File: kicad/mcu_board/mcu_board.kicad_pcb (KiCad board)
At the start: 2 copper layers, 20.3 x 71.1 mm, 25 parts, among them J1 Conn_02x08_Odd_Even, J2 Conn_02x05_Odd_Even, U1 STM32G431CBTx, U2 LD2985BM33R, Y1 ECS-327TXO-33-TR

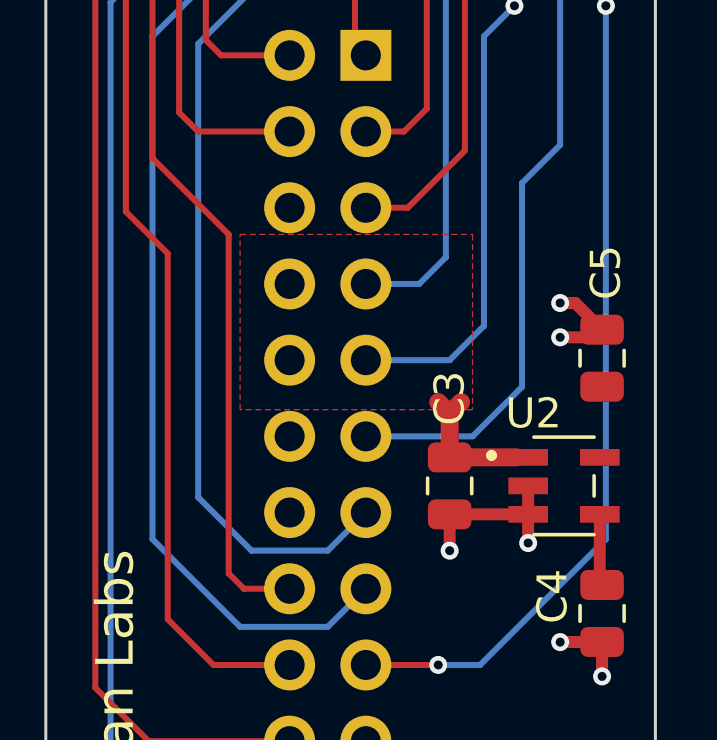
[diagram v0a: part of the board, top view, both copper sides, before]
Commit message: fix LDO bug. FW updates to support new HW
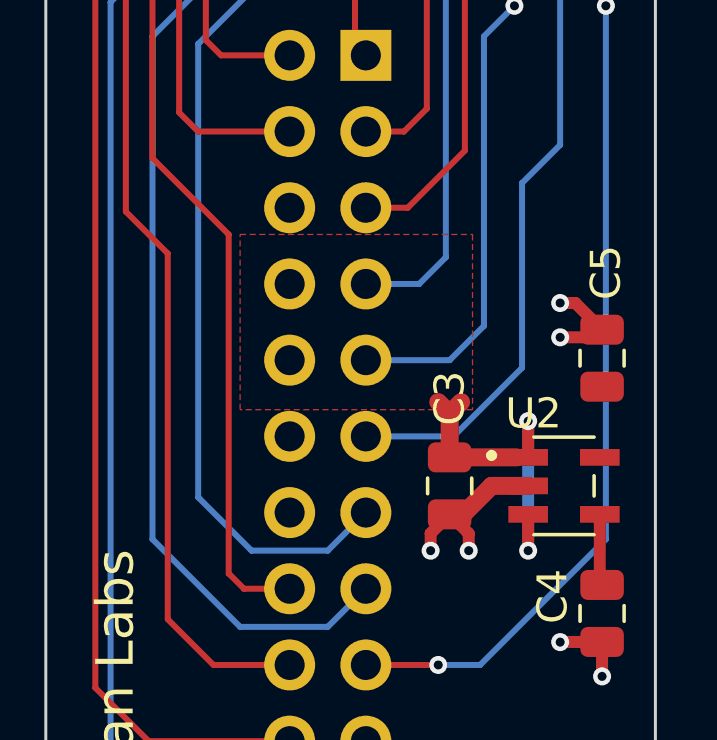
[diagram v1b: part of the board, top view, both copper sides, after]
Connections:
- U2 pad 3: GND -> +5V
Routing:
- net +5V: track 4.78 -> 11.4 mm, vias 0 -> 2
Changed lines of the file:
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@@
       (net 1 "GND") (pinfunction "GND") (pintype "power_in"))
     (pad "3" smd rect (at 1.1938 -0.950001) (size 1.3208 0.5588) (layers "F.Cu" "F.Paste" "F.Mask")
-      (net 1 "GND") (pinfunction "INHIBIT") (pintype "bidirectional"))
+      (net 2 "+5V") (pinfunction "INHIBIT") (pintype "bidirectional"))
     (pad "4" smd rect (at -1.1938 -0.950001) (size 1.3208 0.5588) (layers "F.Cu" "F.Paste" "F.Mask")
       (net 44 "Net-(U2-BYPASS)") (pinfunction "BYPASS") (pintype "unspecified"))
@@
   )
   (segment (start 149.159 68.374) (end 149.111 68.326) (width 0.4) (layer "F.Cu") (net 1))
-  (segment (start 147.193 91.247) (end 147.193 92.456) (width 0.4) (layer "F.Cu") (net 1))
+  (segment (start 148.59 90.297) (end 149.8092 90.297) (width 0.6) (layer "F.Cu") (net 1))
   (segment (start 140.335 55.359) (end 140.335 53.975) (width 0.4) (layer "F.Cu") (net 1))
+  (segment (start 146.558 91.882) (end 147.193 91.247) (width 0.4) (layer "F.Cu") (net 1))
+  (segment (start 146.558 92.456) (end 146.558 91.882) (width 0.4) (layer "F.Cu") (net 1))
   (segment (start 150.876 95.504) (end 150.881 95.499) (width 0.4) (layer "F.Cu") (net 1))
   (segment (start 147.538 64.516) (end 147.538 66.1385) (width 0.3) (layer "F.Cu") (net 1))
@@
   (segment (start 140.335 55.359) (end 141.478 55.359) (width 0.4) (layer "F.Cu") (net 1))
   (segment (start 137.922 53.467) (end 139.253 53.467) (width 0.4) (layer "F.Cu") (net 1))
-  (segment (start 147.193 91.247) (end 149.8092 91.247001) (width 0.4) (layer "F.Cu") (net 1))
+  (segment (start 147.64 91.247) (end 148.59 90.297) (width 0.6) (layer "F.Cu") (net 1))
   (segment (start 136.525 53.467) (end 137.856 53.467) (width 0.4) (layer "F.Cu") (net 1))
   (segment (start 149.032 70.612) (end 149.032 72.009) (width 0.4) (layer "F.Cu") (net 1))
   (segment (start 149.159 70.612) (end 149.159 68.374) (width 0.4) (layer "F.Cu") (net 1))
-  (segment (start 149.8092 91.247001) (end 149.8092 92.202) (width 0.4) (layer "F.Cu") (net 1))
   (segment (start 151.384 84.201) (end 152.273 85.09) (width 0.4) (layer "F.Cu") (net 1))
+  (segment (start 147.193 91.247) (end 147.64 91.247) (width 0.6) (layer "F.Cu") (net 1))
   (segment (start 136.108 61.468) (end 136.108 60.228) (width 0.4) (layer "F.Cu") (net 1))
   (segment (start 150.881 95.499) (end 152.273 95.499) (width 0.4) (layer "F.Cu") (net 1))
@@
   (segment (start 145.034 64.516) (end 145.538 65.024) (width 0.3) (layer "F.Cu") (net 1))
   (segment (start 149.0725 103.124) (end 147.574 103.124) (width 0.2) (layer "F.Cu") (net 1))
+  (segment (start 147.828 92.456) (end 147.828 91.882) (width 0.4) (layer "F.Cu") (net 1))
   (segment (start 150.876 84.201) (end 151.384 84.201) (width 0.4) (layer "F.Cu") (net 1))
-  (segment (start 149.8092 91.247001) (end 149.8092 90.297) (width 0.4) (layer "F.Cu") (net 1))
   (segment (start 149.111 67.678) (end 149.111 68.326) (width 0.4) (layer "F.Cu") (net 1))
   (segment (start 149.606 67.183) (end 149.111 67.678) (width 0.4) (layer "F.Cu") (net 1))
@@
   (segment (start 140.335 53.975) (end 139.827 53.467) (width 0.4) (layer "F.Cu") (net 1))
   (segment (start 150.876 85.344) (end 152.019 85.344) (width 0.4) (layer "F.Cu") (net 1))
+  (segment (start 147.828 91.882) (end 147.193 91.247) (width 0.4) (layer "F.Cu") (net 1))
   (segment (start 152.273 95.499) (end 152.273 96.647) (width 0.4) (layer "F.Cu") (net 1))
   (segment (start 148.173 59.726) (end 149.4505 59.726) (width 0.3) (layer "F.Cu") (net 1))
@@
   (via (at 136.108 61.468) (size 0.6) (drill 0.3) (layers "F.Cu" "B.Cu") (net 1))
   (via (at 151.27 56.007) (size 0.6) (drill 0.3) (layers "F.Cu" "B.Cu") (free) (net 1))
-  (via (at 149.8092 92.202) (size 0.6) (drill 0.3) (layers "F.Cu" "B.Cu") (net 1))
   (via (at 143.51 59.436) (size 0.6) (drill 0.3) (layers "F.Cu" "B.Cu") (free) (net 1))
   (via (at 147.538 64.516) (size 0.6) (drill 0.3) (layers "F.Cu" "B.Cu") (free) (net 1))
@@
   (via (at 147.955 45.085) (size 0.6) (drill 0.3) (layers "F.Cu" "B.Cu") (net 1))
   (via (at 139.319 53.467) (size 0.6) (drill 0.3) (layers "F.Cu" "B.Cu") (free) (net 1))
-  (via (at 147.193 92.456) (size 0.6) (drill 0.3) (layers "F.Cu" "B.Cu") (net 1))
+  (via (at 146.558 92.456) (size 0.6) (drill 0.3) (layers "F.Cu" "B.Cu") (free) (net 1))
+  (via (at 147.828 92.456) (size 0.6) (drill 0.3) (layers "F.Cu" "B.Cu") (free) (net 1))
   (segment (start 147.193 89.347) (end 149.4282 89.346999) (width 0.6) (layer "F.Cu") (net 2))
+  (segment (start 149.8092 89.346999) (end 149.8092 88.138) (width 0.4) (layer "F.Cu") (net 2))
+  (segment (start 149.8092 91.247001) (end 149.8092 92.456) (width 0.4) (layer "F.Cu") (net 2))
   (segment (start 147.193 89.347) (end 147.193 87.884) (width 0.6) (layer "F.Cu") (net 2))
   (segment (start 147.193 87.884) (end 147.574 87.503) (width 0.6) (layer "F.Cu") (net 2))
   (segment (start 147.193 87.884) (end 146.812 87.503) (width 0.6) (layer "F.Cu") (net 2))
+  (via (at 149.8092 92.456) (size 0.6) (drill 0.3) (layers "F.Cu" "B.Cu") (free) (net 2))
+  (via (at 149.8092 88.138) (size 0.6) (drill 0.3) (layers "F.Cu" "B.Cu") (free) (net 2))
+  (segment (start 149.8092 88.138) (end 149.8092 92.329) (width 0.4) (layer "B.Cu") (net 2))
   (segment (start 139.065 75.438) (end 139.065 65.532) (width 0.2) (layer "F.Cu") (net 3))
   (segment (start 139.871 64.726) (end 141.1255 64.726) (width 0.2) (layer "F.Cu") (net 3))
@@
   (segment (start 151.094 64.226) (end 149.4505 64.226) (width 0.2) (layer "F.Cu") (net 11))
   (via (at 150.876 73.406) (size 0.6) (drill 0.3) (layers "F.Cu" "B.Cu") (net 11))
-  (segment (start 149.606 86.995) (end 147.955 88.646) (width 0.2) (layer "B.Cu") (net 11))
+  (segment (start 149.606 86.36) (end 147.32 88.646) (width 0.2) (layer "B.Cu") (net 11))
+  (segment (start 150.876 73.406) (end 150.876 78.9305) (width 0.2) (layer "B.Cu") (net 11))
+  (segment (start 147.32 88.646) (end 144.399 88.646) (width 0.2) (layer "B.Cu") (net 11))
+  (segment (start 149.606 80.2005) (end 149.606 86.36) (width 0.2) (layer "B.Cu") (net 11))
   (segment (start 150.876 78.9305) (end 149.606 80.2005) (width 0.2) (layer "B.Cu") (net 11))
-  (segment (start 149.606 80.2005) (end 149.606 86.995) (width 0.2) (layer "B.Cu") (net 11))
-  (segment (start 147.955 88.646) (end 144.399 88.646) (width 0.2) (layer "B.Cu") (net 11))
-  (segment (start 150.876 73.406) (end 150.876 78.9305) (width 0.2) (layer "B.Cu") (net 11))
   (segment (start 142.24 72.136) (end 143.538 70.838) (width 0.2) (layer "F.Cu") (net 12))
   (segment (start 143.538 70.838) (end 143.538 66.1385) (width 0.2) (layer "F.Cu") (net 12))

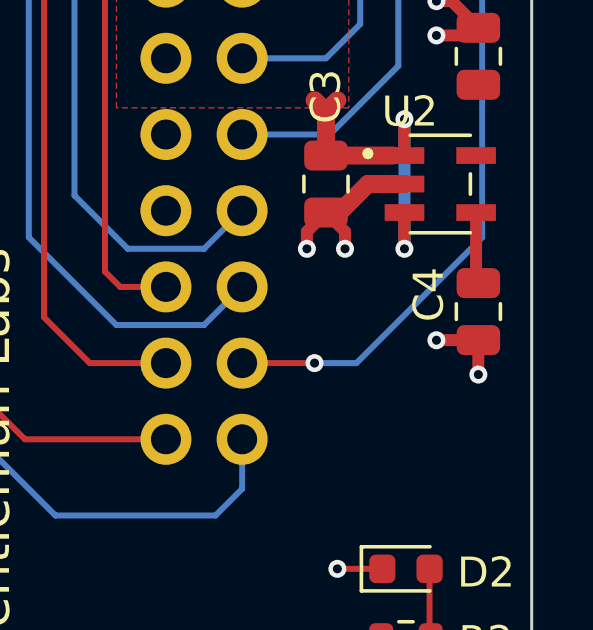
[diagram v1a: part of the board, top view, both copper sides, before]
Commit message: use 100nF 0603 for bypass cap
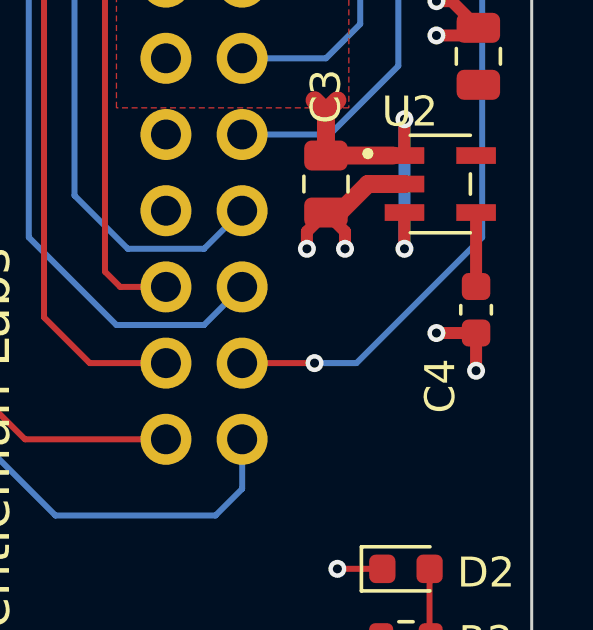
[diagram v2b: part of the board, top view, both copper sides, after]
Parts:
- C4: value 1uF -> 100nF; footprint Capacitor_SMD:C_0805_2012Metric -> Capacitor_SMD:C_0603_1608Metric
- moved C4 0.10 mm to (152.2, 94.5)
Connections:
- C3 pad 2: GND -> Net-(U2-GND)
- U2 pad 2: GND -> Net-(U2-GND)
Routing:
- net Net-(U2-GND): track 0.00 -> 5.95 mm
- net GND: track 35.5 -> 29.6 mm

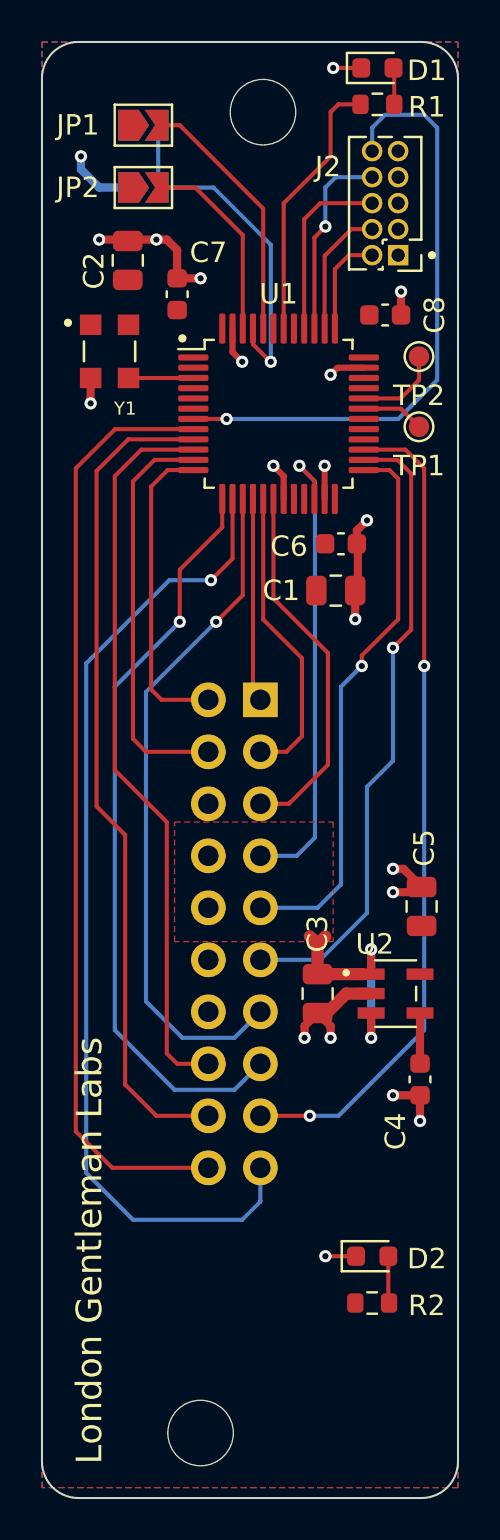
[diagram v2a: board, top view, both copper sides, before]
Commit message: rework LDO section
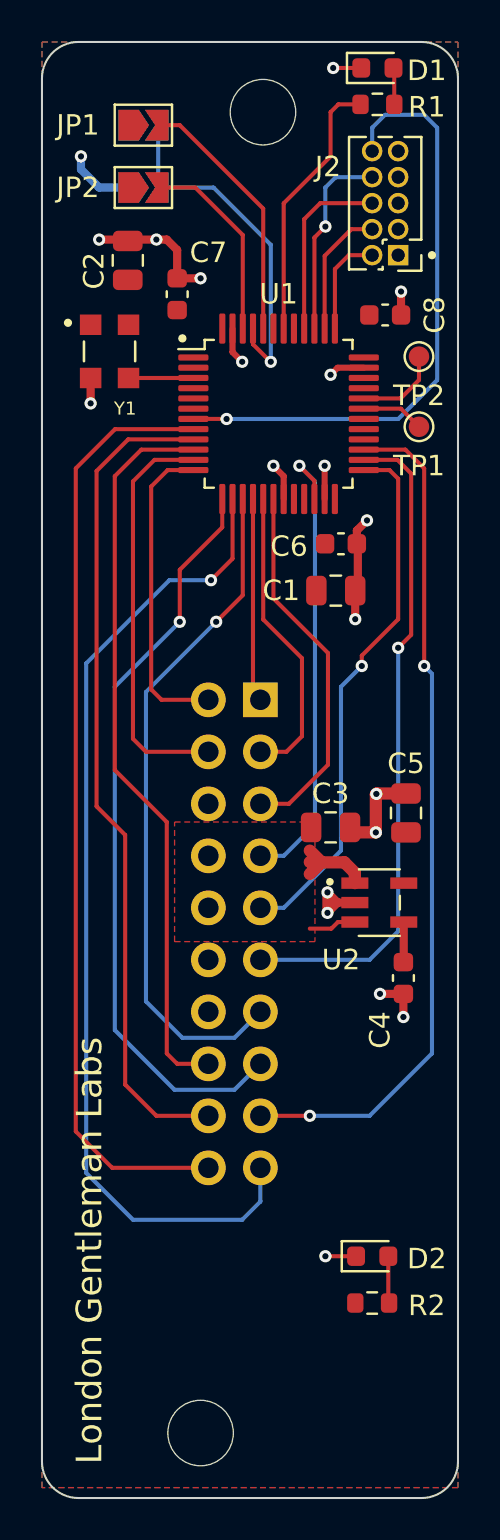
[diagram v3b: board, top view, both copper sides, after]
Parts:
- moved C3 8.14 mm to (147.8, 82.2), turned to 0 degrees
- moved C4 5.02 mm to (151.4, 89.5)
- moved C5 4.63 mm to (151.5, 81.5)
- moved U2 4.52 mm to (150.2, 85.9)
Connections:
- C3 pad 2: Net-(U2-GND) -> GND
- U2 pad 2: Net-(U2-GND) -> GND
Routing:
- net Net-(U2-GND): track 5.95 -> 0.00 mm
- net +5V: track 11.4 -> 6.88 mm, vias 2 -> 0
- net GND: track 29.6 -> 34.0 mm
- net /SPI1_CS_3: track 31.1 -> 32.5 mm
- net /SPI1_CS_4: track 40.5 -> 41.7 mm
- net /SPI1_CS_2: track 27.2 -> 26.3 mm
- net Net-(U2-BYPASS): track 2.47 -> 1.97 mm

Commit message: layout update for LDO
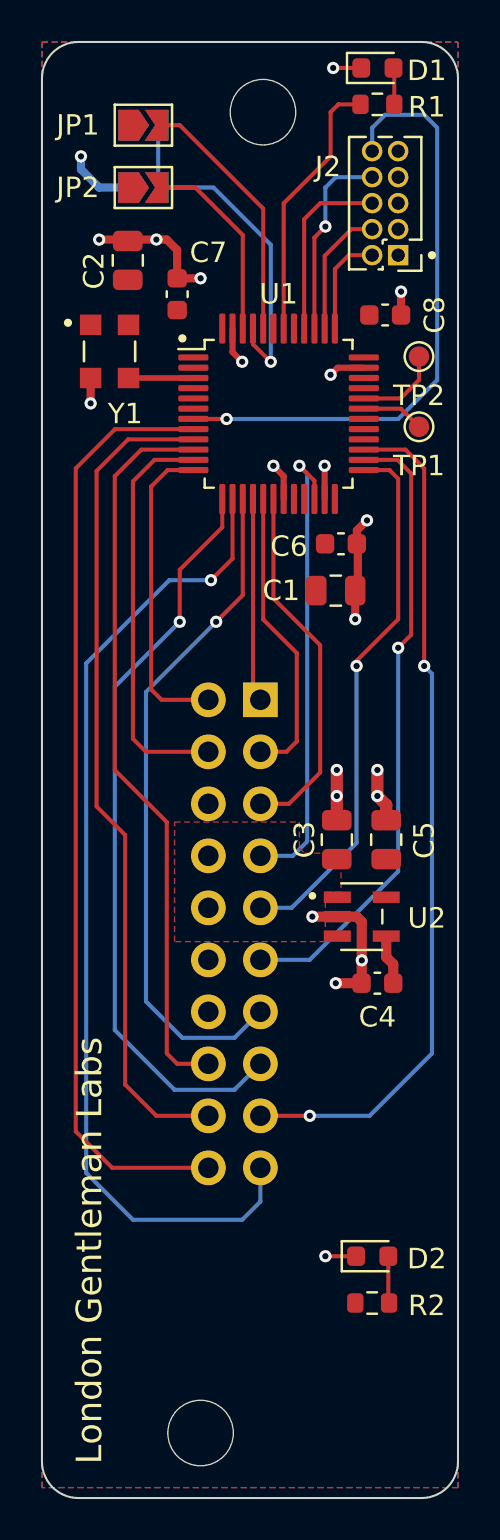
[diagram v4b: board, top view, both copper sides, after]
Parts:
- C4: value 100nF -> 10nF
- moved C5 1.62 mm to (150.5, 82.8)
- moved C4 1.30 mm to (150.1, 89.8), turned to 0 degrees
- moved U2 1.10 mm to (149.4, 86.5)
- moved C3 0.67 mm to (148.1, 82.8), turned to -90 degrees
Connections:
- C3 pad 1: +5V -> GND
- C3 pad 2: GND -> +5V
- C4 pad 1: Net-(U2-BYPASS) -> GND
- C4 pad 2: GND -> Net-(U2-BYPASS)
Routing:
- net +5V: track 6.88 -> 0.00 mm
- net /SPI1_CS_3: track 32.5 -> 30.8 mm
- net GND: track 34.0 -> 35.6 mm, vias 19 -> 20

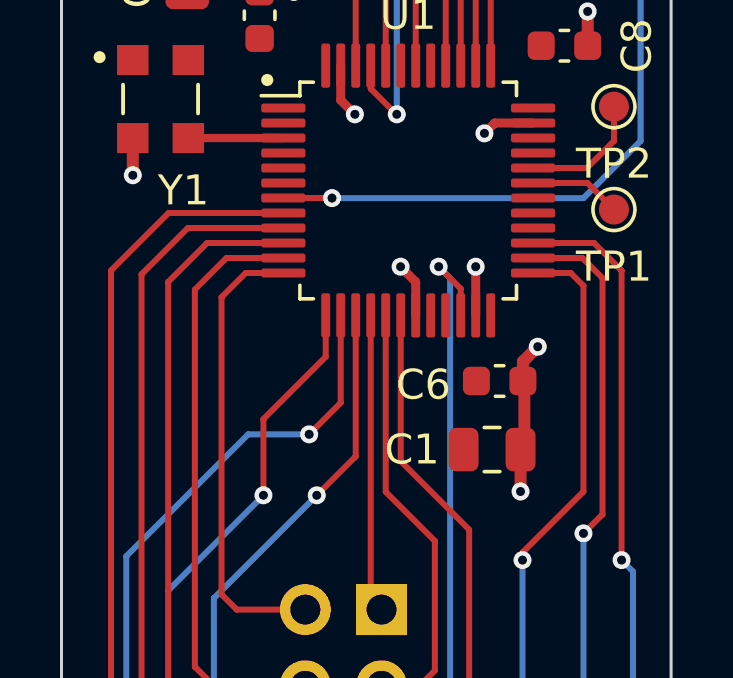
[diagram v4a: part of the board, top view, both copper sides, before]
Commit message: LSCO output on PA2
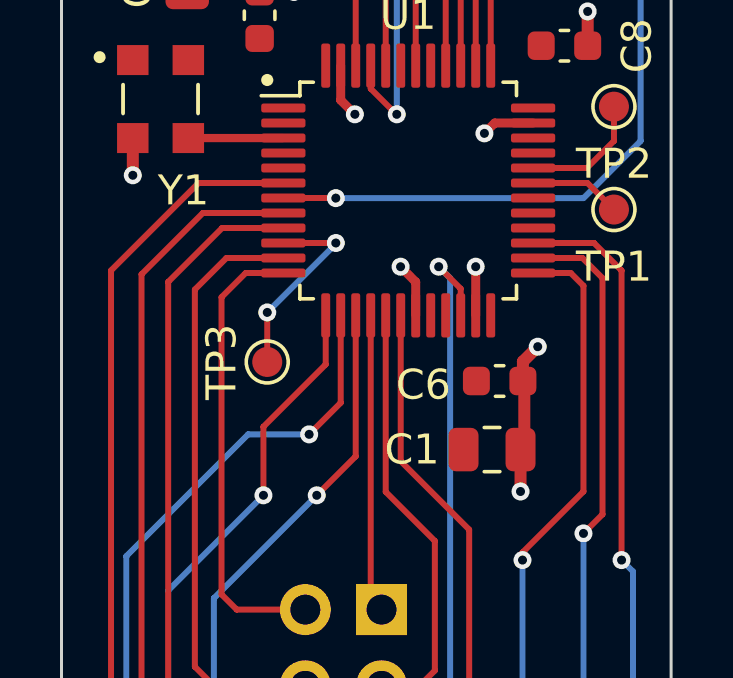
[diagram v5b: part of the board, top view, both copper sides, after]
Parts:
- added TP3: TestPoint, TestPoint:TestPoint_Pad_D1.0mm, F.Cu at (140.6, 67.7)
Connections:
- U1 pad 10: /NCV_EN_2 -> /RCC_LSCO
- U1 pad 6: unconnected-(U1-PF1-OSC_OUT) -> /NCV_EN_4
- U1 pad 8: /NCV_EN_4 -> /NCV_EN_3
- U1 pad 9: /NCV_EN_3 -> /NCV_EN_2
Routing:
- net /RCC_LSCO: track 0.00 -> 6.79 mm, vias 0 -> 2
